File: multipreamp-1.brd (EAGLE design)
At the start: 100 x 50 mm, 114 parts, among them Q1 J201, Q2 J201, Q3 J201, Q4 J201, Q5 2N5088, Q6 J201, Q7 J201

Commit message: Ajustes no esquematico e no layout
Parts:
- removed C5, C6, C7: (no value), rcl:C050-025X075
- removed JP6, JP7: (no value), pinhead:1X01
- removed R10, R7, R8, R9: (no value), rcl:0207/7
- added SJ3, SJ4: (no value), jumper:SJ
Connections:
- removed net N$41: C22.1, C23.1, R38.1
- removed net N$7: C2.1, C5.2, R8.1
- removed net N$9: C6.1, C7.1, R10.1, R8.2
- new net TONE_IN: C22.1, C23.1, R38.1, SJ3.2
- new net TONE_OUT: POT_TONE/TREBLE.2, SJ4.1
- net GND: no longer C6.2, JP7.1, R7.2, R9.1
- net N$11: now also SJ4.2; no longer POT_TONE/TREBLE.2
- net N$6: now also C2.1, SJ3.1; no longer C7.2, JP6.1, R9.2
- net TONE/TREBLE_1: no longer R10.2
- net TONE/TREBLE_3: no longer C5.1, R7.1
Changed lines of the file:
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@@
 <element name="R5" library="rcl" package="0207/7" value="" x="57.15" y="17.78" rot="R90"/>
 <element name="R6" library="rcl" package="RTRIM64W" value="" x="13.97" y="26.67" rot="R90"/>
-<element name="C5" library="rcl" package="C050-025X075" value="" x="62.23" y="7.62" rot="R90"/>
-<element name="C6" library="rcl" package="C050-025X075" value="" x="67.31" y="7.62" rot="R90"/>
-<element name="R7" library="rcl" package="0207/7" value="" x="72.39" y="8.89" rot="R90"/>
-<element name="R8" library="rcl" package="0207/7" value="" x="77.47" y="8.89" rot="R90"/>
-<element name="C7" library="rcl" package="C050-025X075" value="" x="82.55" y="7.62" rot="R90"/>
-<element name="R9" library="rcl" package="0207/7" value="" x="87.63" y="8.89" rot="R90"/>
-<element name="R10" library="rcl" package="0207/7" value="" x="92.71" y="8.89" rot="R90"/>
 <element name="POT_TONE/TREBLE" library="gm-pots" package="16MM-PCB-MOUNT" value="" x="29.21" y="45.72"/>
 <element name="POT_GAIN" library="gm-pots" package="16MM-PCB-MOUNT" value="" x="8.89" y="45.72"/>
@@
 <element name="JP4" library="pinhead" package="1X01" value="" x="-115.57" y="-313.69"/>
 <element name="JP5" library="pinhead" package="1X01" value="" x="-115.57" y="-318.77"/>
-<element name="JP6" library="pinhead" package="1X01" value="" x="-115.57" y="-323.85"/>
-<element name="JP7" library="pinhead" package="1X01" value="" x="-115.57" y="-328.93"/>
 <element name="R37" library="rcl" package="0207/7" value="" x="-113.03" y="-334.01"/>
 <element name="JP_IN" library="pinhead" package="1X01" value="" x="6.35" y="6.35"/>
@@
 </element>
 <element name="SJ2" library="jumper" package="SJ" value="" x="-172.72" y="-515.62"/>
+<element name="SJ3" library="jumper" package="SJ" value="" x="-172.72" y="-520.7"/>
+<element name="SJ4" library="jumper" package="SJ" value="" x="-172.72" y="-525.78"/>
 </elements>
 <signals>
@@
 <contactref element="R4" pad="1"/>
 <contactref element="R5" pad="1"/>
-<contactref element="R9" pad="1"/>
-<contactref element="C6" pad="2"/>
-<contactref element="R7" pad="2"/>
 <contactref element="R11" pad="1"/>
 <contactref element="R13" pad="1"/>
@@
 <contactref element="POT_VOL" pad="1"/>
 <contactref element="JP5" pad="1"/>
-<contactref element="JP7" pad="1"/>
 <contactref element="R37" pad="1"/>
 <contactref element="R3" pad="1"/>
@@
 <wire x1="-97.79" y1="-308.61" x2="-90.17" y2="-288.29" width="0" layer="19" extent="1-1"/>
 <wire x1="-115.57" y1="-318.77" x2="-97.79" y2="-308.61" width="0" layer="19" extent="1-1"/>
-<wire x1="-115.57" y1="-328.93" x2="-115.57" y2="-318.77" width="0" layer="19" extent="1-1"/>
-<wire x1="-116.84" y1="-334.01" x2="-115.57" y2="-328.93" width="0" layer="19" extent="1-1"/>
+<wire x1="-116.84" y1="-334.01" x2="-115.57" y2="-318.77" width="0" layer="19" extent="1-1"/>
 <wire x1="-115.57" y1="-354.33" x2="-116.84" y2="-334.01" width="0" layer="19" extent="1-1"/>
 <wire x1="-166.37" y1="-384.81" x2="-115.57" y2="-354.33" width="0" layer="19" extent="1-1"/>
@@
 <wire x1="46.99" y1="13.97" x2="6.35" y2="2.54" width="0" layer="19" extent="1-1"/>
 <wire x1="57.15" y1="13.97" x2="46.99" y2="13.97" width="0" layer="19" extent="1-1"/>
-<wire x1="67.31" y1="10.16" x2="57.15" y2="13.97" width="0" layer="19" extent="1-1"/>
-<wire x1="72.39" y1="12.7" x2="67.31" y2="10.16" width="0" layer="19" extent="1-1"/>
-<wire x1="87.63" y1="5.08" x2="72.39" y2="12.7" width="0" layer="19" extent="1-1"/>
 <wire x1="54.61" y1="45.72" x2="57.15" y2="13.97" width="0" layer="19" extent="1-1"/>
 <wire x1="49.53" y1="45.72" x2="54.61" y2="45.72" width="0" layer="19" extent="1-1"/>
-<wire x1="95.25" y1="45.72" x2="72.39" y2="12.7" width="0" layer="19" extent="1-1"/>
+<wire x1="95.25" y1="45.72" x2="54.61" y2="45.72" width="0" layer="19" extent="1-1"/>
 </signal>
 <signal name="N$1">
@@
 <wire x1="6.35" y1="6.35" x2="6.03" y2="10.16" width="0" layer="19" extent="1-1"/>
 </signal>
-<signal name="N$6">
-<contactref element="C7" pad="2"/>
-<contactref element="R9" pad="2"/>
-<contactref element="JP6" pad="1"/>
-<wire x1="82.55" y1="10.16" x2="-115.57" y2="-323.85" width="0" layer="19" extent="1-1"/>
-<wire x1="87.63" y1="12.7" x2="82.55" y2="10.16" width="0" layer="19" extent="1-1"/>
-</signal>
-<signal name="N$7">
-<contactref element="C5" pad="2"/>
-<contactref element="R8" pad="1"/>
-<contactref element="C2" pad="1"/>
-<wire x1="77.47" y1="5.08" x2="77.47" y2="26.67" width="0" layer="19" extent="1-1"/>
-<wire x1="62.23" y1="10.16" x2="77.47" y2="5.08" width="0" layer="19" extent="1-1"/>
-</signal>
-<signal name="N$9">
-<contactref element="R8" pad="2"/>
-<contactref element="C6" pad="1"/>
-<contactref element="C7" pad="1"/>
-<contactref element="R10" pad="1"/>
-<wire x1="82.55" y1="5.08" x2="92.71" y2="5.08" width="0" layer="19" extent="1-1"/>
-<wire x1="77.47" y1="12.7" x2="82.55" y2="5.08" width="0" layer="19" extent="1-1"/>
-<wire x1="67.31" y1="5.08" x2="77.47" y2="12.7" width="0" layer="19" extent="1-1"/>
-</signal>
 <signal name="N$11">
-<contactref element="POT_TONE/TREBLE" pad="2"/>
 <contactref element="POT_GAIN" pad="3"/>
 <contactref element="C33" pad="2"/>
+<contactref element="SJ4" pad="2"/>
+<wire x1="-170.18" y1="-500.38" x2="-171.958" y2="-525.78" width="0" layer="19" extent="1-1"/>
 <wire x1="3.81" y1="45.72" x2="-170.18" y2="-500.38" width="0" layer="19" extent="1-1"/>
-<wire x1="29.21" y1="45.72" x2="3.81" y2="45.72" width="0" layer="19" extent="1-1"/>
 </signal>
 <signal name="N$12">
@@
 <contactref element="POT_BASS" pad="2"/>
 <contactref element="C24" pad="1"/>
-<contactref element="R10" pad="2"/>
 <contactref element="POT_TONE/TREBLE" pad="1"/>
 <wire x1="64.77" y1="45.72" x2="69.85" y2="45.72" width="0" layer="19" extent="1-1"/>
 <wire x1="34.29" y1="45.72" x2="64.77" y2="45.72" width="0" layer="19" extent="1-1"/>
-<wire x1="92.71" y1="12.7" x2="69.85" y2="45.72" width="0" layer="19" extent="1-1"/>
-<wire x1="-172.72" y1="-389.89" x2="92.71" y2="12.7" width="0" layer="19" extent="1-1"/>
+<wire x1="-172.72" y1="-389.89" x2="34.29" y2="45.72" width="0" layer="19" extent="1-1"/>
 </signal>
 <signal name="N$37">
@@
 <wire x1="-173.482" y1="-394.97" x2="-172.72" y2="-379.73" width="0" layer="19" extent="1-1"/>
 </signal>
-<signal name="N$39">
-<contactref element="R38" pad="2"/>
-<contactref element="C25" pad="2"/>
-<contactref element="C24" pad="2"/>
-<wire x1="-167.64" y1="-379.73" x2="-167.64" y2="-389.89" width="0" layer="19" extent="1-1"/>
-<wire x1="-166.37" y1="-369.57" x2="-167.64" y2="-379.73" width="0" layer="19" extent="1-1"/>
-</signal>
 <signal name="TONE/TREBLE_3">
 <contactref element="C23" pad="2"/>
 <contactref element="C22" pad="2"/>
-<contactref element="C5" pad="1"/>
-<contactref element="R7" pad="1"/>
 <contactref element="POT_TONE/TREBLE" pad="3"/>
-<wire x1="62.23" y1="5.08" x2="72.39" y2="5.08" width="0" layer="19" extent="1-1"/>
-<wire x1="24.13" y1="45.72" x2="62.23" y2="5.08" width="0" layer="19" extent="1-1"/>
-<wire x1="-170.18" y1="-359.41" x2="62.23" y2="5.08" width="0" layer="19" extent="1-1"/>
+<wire x1="-170.18" y1="-359.41" x2="24.13" y2="45.72" width="0" layer="19" extent="1-1"/>
 <wire x1="-170.18" y1="-364.49" x2="-170.18" y2="-359.41" width="0" layer="19" extent="1-1"/>
-</signal>
-<signal name="N$41">
-<contactref element="C23" pad="1"/>
-<contactref element="C22" pad="1"/>
-<contactref element="R38" pad="1"/>
-<wire x1="-172.72" y1="-364.49" x2="-173.99" y2="-369.57" width="0" layer="19" extent="1-1"/>
-<wire x1="-172.72" y1="-359.41" x2="-172.72" y2="-364.49" width="0" layer="19" extent="1-1"/>
 </signal>
 <signal name="N$43">
@@
 <wire x1="-78.74" y1="-82.55" x2="-77.47" y2="-87.63" width="0" layer="19" extent="1-1"/>
 </signal>
+<signal name="N$36">
+<contactref element="R38" pad="2"/>
+<contactref element="C25" pad="2"/>
+<contactref element="C24" pad="2"/>
+<wire x1="-167.64" y1="-379.73" x2="-167.64" y2="-389.89" width="0" layer="19" extent="1-1"/>
+<wire x1="-166.37" y1="-369.57" x2="-167.64" y2="-379.73" width="0" layer="19" extent="1-1"/>
+</signal>
+<signal name="N$6">
+<contactref element="C2" pad="1"/>
+<contactref element="SJ3" pad="1"/>
+<wire x1="77.47" y1="26.67" x2="-173.482" y2="-520.7" width="0" layer="19" extent="1-1"/>
+</signal>
+<signal name="TONE_IN">
+<contactref element="SJ3" pad="2"/>
+<contactref element="C23" pad="1"/>
+<contactref element="C22" pad="1"/>
+<contactref element="R38" pad="1"/>
+<wire x1="-173.99" y1="-369.57" x2="-171.958" y2="-520.7" width="0" layer="19" extent="1-1"/>
+<wire x1="-172.72" y1="-364.49" x2="-173.99" y2="-369.57" width="0" layer="19" extent="1-1"/>
+<wire x1="-172.72" y1="-359.41" x2="-172.72" y2="-364.49" width="0" layer="19" extent="1-1"/>
+</signal>
+<signal name="TONE_OUT">
+<contactref element="SJ4" pad="1"/>
+<contactref element="POT_TONE/TREBLE" pad="2"/>
+<wire x1="29.21" y1="45.72" x2="-173.482" y2="-525.78" width="0" layer="19" extent="1-1"/>
+</signal>
 </signals>

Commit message: Desenvolvimento do layout - roteamento da placa Pendente roteamento do terra e análises do esquematico e layout
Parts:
- removed JP12, JP13, JP14, JP4, JP5: (no value), pinhead:1X01
- added C5: (no value), rcl:C050-025X075
- added C6: (no value), rcl:E2,5-6
- added C7: 100n SMD, rcl:C0805
- added JP+, JP-, JP6, JP7, JP_BRT1, JP_BRT2: (no value), pinhead:1X01
- added Q8: J201, gm-trans:TO92-
- added R7: (no value), rcl:0207/5V
- added R8, R9: (no value), rcl:0207/7
- added SJ5: (no value), jumper:SJ
- R19: device rcl:0207/7 -> rcl:0207/5V
- moved SJ4 602.9 mm to (26.7, 43.2), flipped to the bottom, turned to 270 degrees
- moved SJ2 591.4 mm to (80.0, 19.1), flipped to the bottom, turned to 180 degrees
- moved TP2 575.9 mm to (62.2, 15.2)
- moved C33 571.1 mm to (15.2, 39.4), turned to 180 degrees
- moved SJ3 566.7 mm to (15.2, 14.0), flipped to the bottom, turned to 180 degrees
- moved C32 559.5 mm to (83.8, 3.81), turned to 270 degrees
- moved TP1 556.4 mm to (16.5, 17.8)
- moved C31 542.1 mm to (57.1, 3.81), turned to 270 degrees
- moved C30 527.5 mm to (35.6, 3.81), turned to 270 degrees
- moved C29 513.7 mm to (24.1, 16.5), turned to 270 degrees
- moved C28 507.3 mm to (21.6, 16.5), flipped to the bottom, turned to 270 degrees
- moved R43 503.7 mm to (27.3, 16.5), flipped to the bottom, turned to 270 degrees
- moved R42 502.0 mm to (27.3, 21.0), flipped to the bottom, turned to 270 degrees
- moved R39 496.8 mm to (80.0, 44.5), turned to 90 degrees
- moved R41 495.9 mm to (44.5, 12.7), flipped to the bottom
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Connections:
- removed net N$34: C20.2, POT_VOL.3, R36.2, R37.2
- new net N$14: C5.1, JP7.1
- new net N$7: C26.+, Q6.1, R40.1, R7.1
- new net N$9: C20.2, POT_VOL.3, R36.2, R37.2, R9.1, SJ5.2
- net GND: now also C3.2, C6.-, C7.2, JP-.1, JP6.1, JP_BRT2.1, R8.1; no longer JP12.1, JP13.1, JP14.1, JP5.1
- net N$1: now also JP_BRT1.1; no longer JP4.1
- net N$10: now also C5.2, R9.2; no longer C26.+, Q6.1, R40.1
- net N$28: now also Q8.1
- net TONE_IN: now also Q8.2, R8.2
- net TONE_OUT: now also SJ5.1
- net V+: now also C3.1, C6.+, C7.1, JP+.1, Q8.3
- net VCC/2: now also R7.2
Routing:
- net V+: track 0.00 -> 113.7 mm
- net TONE_IN: track 0.00 -> 84.5 mm, vias 0 -> 2
- net N$9: track 0.00 -> 76.5 mm
- net TONE/TREBLE_1: track 0.00 -> 51.1 mm
- net VCC/2: track 0.00 -> 39.5 mm, vias 0 -> 1
- net N$43: track 0.00 -> 38.4 mm, vias 0 -> 1
- net N$11: track 0.00 -> 30.0 mm
- net N$8: track 0.00 -> 29.2 mm
- net N$13: track 0.00 -> 29.1 mm
- net N$28: track 0.00 -> 28.8 mm
- net N$15: track 0.00 -> 25.4 mm
- net N$42: track 0.00 -> 25.2 mm
- net N$19: track 0.00 -> 20.8 mm
- net N$25: track 0.00 -> 20.1 mm
- net N$32: track 0.00 -> 17.3 mm
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
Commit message: Revisao do esquematico
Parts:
- added SJ6: (no value), jumper:SJ
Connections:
- net N$11: now also SJ6.2
- net N$6: now also SJ6.1
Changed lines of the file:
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@@
 <element name="C6" library="rcl" package="E2,5-6" value="" x="5.08" y="36.83" rot="R180"/>
 <element name="C7" library="rcl" package="C0805" value="100n SMD" x="66.04" y="29.21" rot="MR90"/>
+<element name="SJ6" library="jumper" package="SJ" value="" x="15.24" y="35.56" rot="MR90"/>
 </elements>
 <signals>
@@
 <wire x1="4.572" y1="42.418" x2="3.81" y2="43.18" width="0.6096" layer="16" curve="-90"/>
 <wire x1="13.97" y1="39.37" x2="13.97" y2="42.418" width="0.6096" layer="16"/>
+<contactref element="SJ6" pad="2"/>
+<wire x1="15.24" y1="36.322" x2="13.97" y2="39.37" width="0" layer="19" extent="16-16"/>
 </signal>
 <signal name="N$12">
@@
 <wire x1="14.478" y1="13.97" x2="13.97" y2="13.97" width="0.6096" layer="16"/>
 <wire x1="13.97" y1="13.97" x2="12.7" y2="12.7" width="0.6096" layer="16" curve="90"/>
+<contactref element="SJ6" pad="1"/>
+<wire x1="14.478" y1="13.97" x2="15.24" y2="34.798" width="0" layer="19" extent="16-16"/>
 </signal>
 <signal name="TONE_IN">

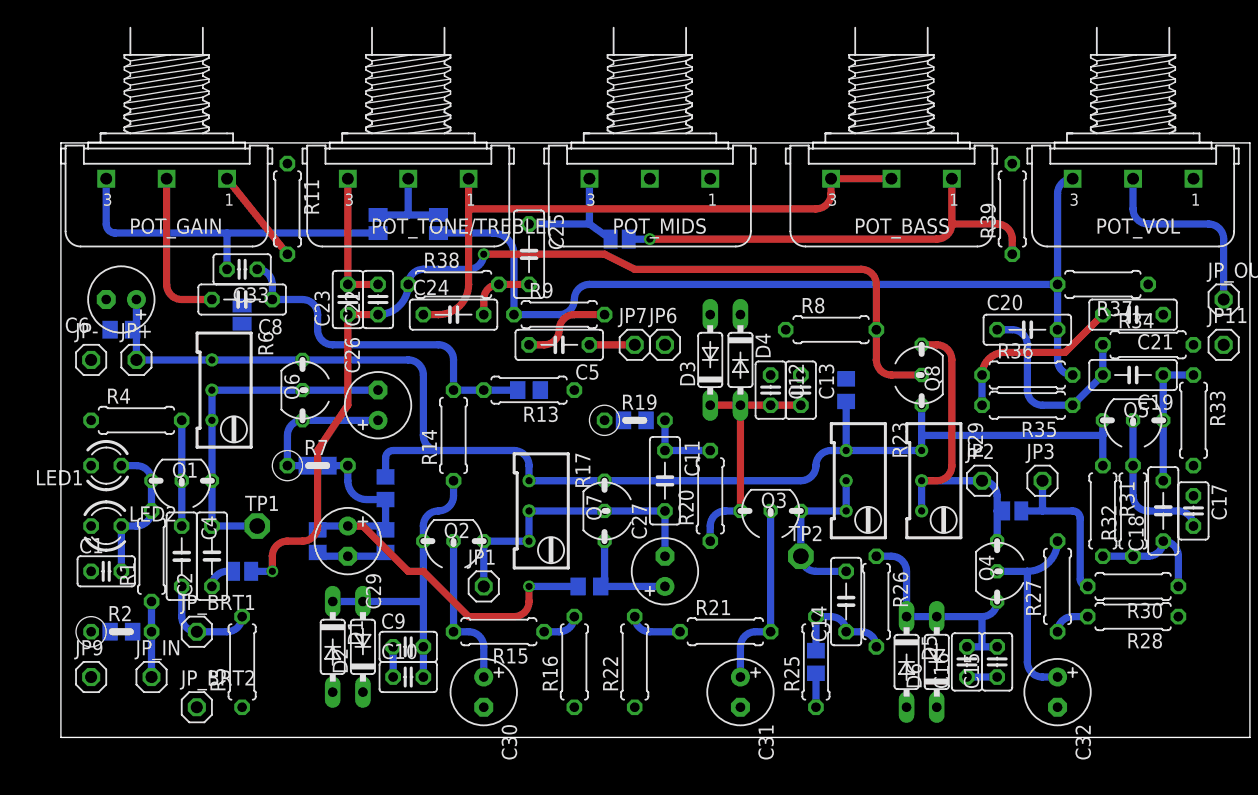
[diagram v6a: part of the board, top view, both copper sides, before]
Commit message: Alteracoes e correcoes no esquematico e layout apos verificacao para montagem de Azabache/Spitfire/Dr Boogie
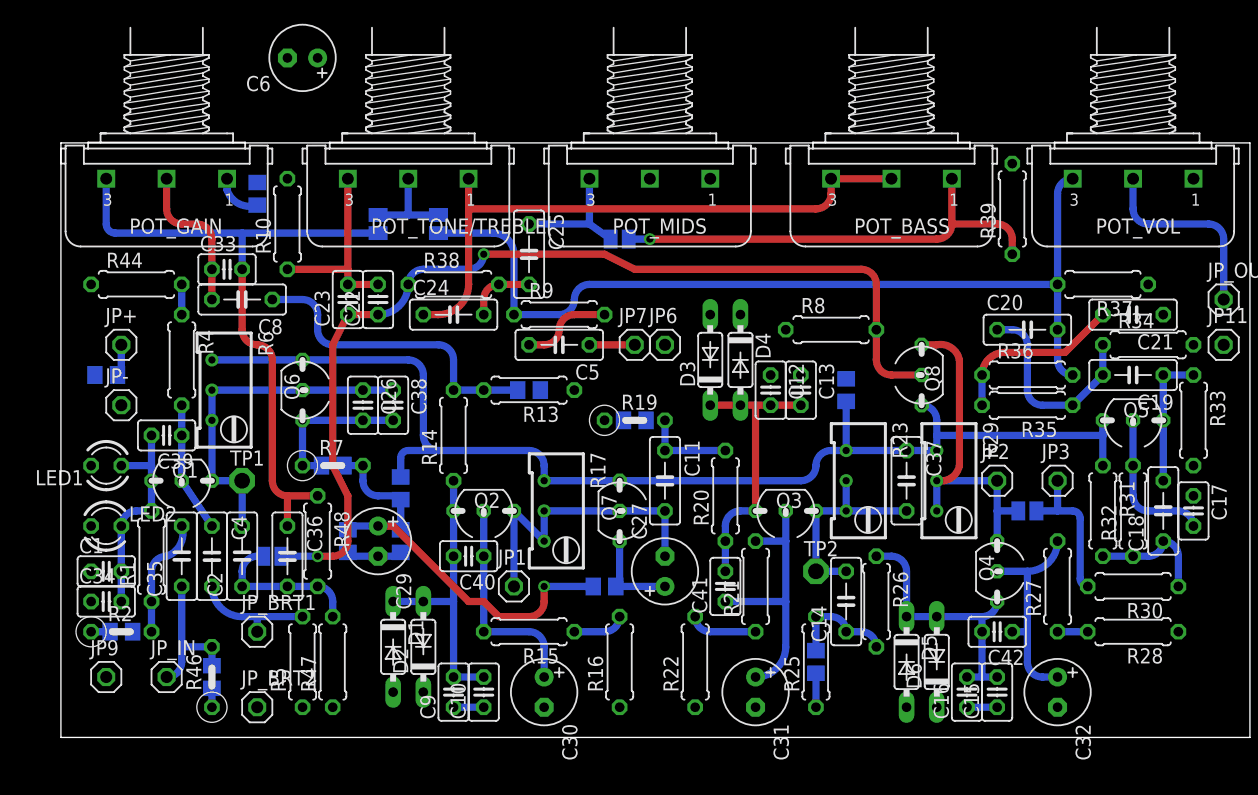
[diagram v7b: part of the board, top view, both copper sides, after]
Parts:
- removed SJ6: (no value), jumper:SJ
- added C34, C38, C39, C40, C41, C42: (no value), rcl:C025-025X050
- added C35, C36, C37: (no value), rcl:C050-025X075
- added R10, R44, R47, R48: (no value), rcl:0207/7
- added R45: 1M SMD, rcl:R0805
- added R46: (no value), rcl:0207/5V
- C26: device rcl:E2,5-6 -> rcl:C025-025X050
- R11: device rcl:0207/7 -> rcl:R0805
- moved C6 25.4 mm to (20.3, 57.1)
- moved C10 6.48 mm to (35.6, 3.81), turned to 90 degrees
- moved R4 6.35 mm to (10.2, 31.8), turned to 270 degrees
- moved C9 5.39 mm to (33.0, 3.81), turned to 90 degrees
- moved R22 5.08 mm to (53.3, 6.35)
- moved D1 5.08 mm to (27.9, 7.62)
- moved D2 5.08 mm to (30.5, 7.62)
- moved JP_BRT1 5.08 mm to (16.5, 8.89)
- moved JP_BRT2 5.08 mm to (16.5, 2.54)
- moved R5 5.08 mm to (20.3, 6.35)
- moved C30 5.08 mm to (40.6, 3.81)
- moved JP- 4.58 mm to (5.08, 27.9)
- moved R21 4.58 mm to (58.4, 12.7), turned to 90 degrees
- moved C3 4.02 mm to (3.81, 30.5)
- moved TP1 4.02 mm to (15.2, 21.6)
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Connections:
- removed net N$6: C2.1, SJ3.1, SJ6.1
- new net N$34: R4.1, R44.2
- new net N$38: C35.1, JP_IN.1, R45.2, R46.2
- new net N$39: C2.1, C36.2, R47.2, R48.2, SJ3.1
- net GND: now also C34.1, R10.2, R44.1, R45.1, R46.1, R47.1; no longer R4.1
- net N$11: now also C36.1, R48.1; no longer SJ6.2
- net N$13: no longer C33.1
- net N$16: now also C40.1
- net N$19: now also C41.2
- net N$2: now also C39.1
- net N$20: now also C41.1
- net N$22: now also C37.2
- net N$25: now also C42.2
- net N$26: now also C42.1
- net N$3: now also C33.1
- net N$4: now also C34.2, C39.2
- net N$42: now also C40.2
- net N$5: now also C35.2; no longer JP_IN.1
- net N$7: now also C26.2, C38.2; no longer C26.+
- net N$8: now also C26.1, C38.1; no longer C26.-
- net TONE/TREBLE_3: now also R10.1
- net V+: now also C37.1
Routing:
- net N$11: track 30.0 -> 55.7 mm
- net N$39: track 0.00 -> 13.0 mm
- net N$38: track 0.00 -> 12.3 mm
- net V+: track 113.7 -> 104.1 mm
- net N$20: track 15.8 -> 22.6 mm
- net N$4: track 12.5 -> 18.3 mm
- net N$16: track 13.2 -> 18.3 mm
- net TONE/TREBLE_3: track 11.4 -> 16.5 mm
- net N$12: track 8.13 -> 3.79 mm
- net N$5: track 6.35 -> 9.72 mm
- net N$22: track 14.5 -> 17.8 mm
- net N$13: track 29.1 -> 26.0 mm
- net N$19: track 20.8 -> 23.4 mm
- net VCC/2: track 39.5 -> 37.0 mm
- net N$34: track 0.00 -> 2.54 mm
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
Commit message: Ajustes no tonestack para contemplar montagens Fender/Marshall/Dumble
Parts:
- added SJ6: (no value), jumper:SJ
- moved JP- 92.1 mm to (94.0, 3.81)
- moved JP+ 88.8 mm to (88.9, 3.81)
- moved C25 4.58 mm to (43.2, 38.1), turned to 180 degrees
- moved SJ1 4.02 mm to (43.2, 43.2), turned to 270 degrees
- moved R12 2.54 mm to (39.4, 26.7)
- moved R13 2.54 mm to (39.4, 26.7)
- moved Q4 2.54 mm to (76.2, 14.0), turned to 180 degrees
- moved C5 1.80 mm to (40.6, 31.8)
- moved JP7 1.80 mm to (47.0, 31.8)
- moved JP6 1.27 mm to (50.8, 31.8)
- moved R9 1.27 mm to (41.9, 34.3)
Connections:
- new net N$6: C25.1, POT_MIDS.2, SJ6.2
- net GND: no longer POT_MIDS.2
- net N$37: now also SJ6.1; no longer C25.1
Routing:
- net V+: track 104.1 -> 86.3 mm
- net N$6: track 0.00 -> 13.0 mm
- net N$37: track 11.1 -> 5.35 mm
- net N$43: track 38.4 -> 43.5 mm
- net N$14: track 3.81 -> 0.00 mm
- net N$28: track 29.2 -> 31.8 mm
- net N$26: track 18.1 -> 16.3 mm
- net N$36: track 5.61 -> 6.88 mm
- net N$25: track 22.6 -> 23.9 mm
- net N$10: track 7.40 -> 8.67 mm
- net N$13: track 26.0 -> 27.1 mm
- net N$9: track 76.5 -> 77.2 mm
